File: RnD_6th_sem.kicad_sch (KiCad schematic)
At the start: 62 parts, among them IC1 2EDF7275KXUMA1, J1 HVDC, J10 MMCX-J-P-H-ST-TH1, J2 PWM, J3 HVDC, J4 Conn_02x05_Odd_Even, J5 5V, J6 5V, J7 GND, J8 GND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

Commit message: Final design
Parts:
- removed J4: Conn_02x05_Odd_Even, 61201021621:SHDR10W64P254_2X5_2036X885X925P, symbol Connector_Generic:Conn_02x05_Odd_Even
- added J4: Conn_02x03_Odd_Even, Connector_PinSocket_2.54mm:PinSocket_2x03_P2.54mm_Horizontal, symbol Connector_Generic:Conn_02x03_Odd_Even
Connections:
- net +3.3V: now also J4.1 (Pin_1)
- net GND: now also J4.2 (Pin_2)
- net GND1: now also J4.6 (Pin_6)
- net GND2: now also J4.4 (Pin_4)
- net VCCA: now also J4.5 (Pin_5)
- net VCCB: now also J4.3 (Pin_3)
- no-connect marks 4 -> 0

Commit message: updated the SLDO conn.
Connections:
- net GND: no longer IC1.4 (SLDON)
- no-connect marks 0 -> 1
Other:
- note removed: "Test points: 1. for both current sense resistors 2. High side gan, between them, low side of gan"
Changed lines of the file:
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@@
   (junction (at 177.8 37.465) (diameter 0) (color 0 0 0 0)
   )
+  (no_connect (at 121.285 37.465))
   (wire (pts (xy 98.425 130.175) (xy 101.6 130.175))
     (stroke (width 0) (type default))
@@
     (stroke (width 0) (type default))
   )
-  (wire (pts (xy 97.155 37.465) (xy 121.285 37.465))
-    (stroke (width 0) (type default))
-  )
   (wire (pts (xy 183.515 35.56) (xy 183.515 37.465))
     (stroke (width 0) (type default))
@@
     (stroke (width 0) (type default))
   )
-  (text "Test points: \n1. for both current sense resistors\n2. High side gan, between them, low side of gan\n"
-    (at 221.615 149.225 0)
-    (effects (font (size 1.27 1.27)) (justify left bottom))
-  )
   (text "LEDs" (at 31.75 69.215 0)

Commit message: changed TPs location
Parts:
- added TP6: TestPoint_Alt, TestPoint:TestPoint_Keystone_5000-5004_Miniature, symbol Connector:TestPoint_Alt
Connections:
- net GND3: now also TP6.1
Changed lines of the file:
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@@
   (junction (at 132.08 107.315) (diameter 0) (color 0 0 0 0)
+  )
+  (junction (at 167.005 151.13) (diameter 0) (color 0 0 0 0)
   )
   (junction (at 98.425 133.985) (diameter 0) (color 0 0 0 0)
@@
     (stroke (width 0) (type default))
   )
+  (wire (pts (xy 167.005 151.13) (xy 167.005 157.48))
+    (stroke (width 0) (type default))
+  )
   (wire (pts (xy 192.405 52.705) (xy 198.12 52.705))
     (stroke (width 0) (type default))
@@
     (stroke (width 0) (type default))
   )
-  (wire (pts (xy 167.005 99.06) (xy 167.005 157.48))
+  (wire (pts (xy 167.005 99.06) (xy 167.005 151.13))
     (stroke (width 0) (type default))
   )
@@
         )
       )
+    )
+  )
+  (symbol (lib_id "Connector:TestPoint_Alt") (at 167.005 151.13 270) (unit 1)
+    (in_bom yes) (on_board yes) (dnp no)
+    (property "Reference" "TP6" (at 168.91 153.035 0)
+      (effects (font (size 1.27 1.27)))
+    )
+    (property "Value" "TestPoint_Alt" (at 172.085 153.035 0)
+      (effects (font (size 1.27 1.27)))
+    )
+    (property "Footprint" "TestPoint:TestPoint_Keystone_5000-5004_Miniature" (at 167.005 156.21 0)
+      (effects (font (size 1.27 1.27)) hide)
+    )
+    (property "Datasheet" "~" (at 167.005 156.21 0)
+      (effects (font (size 1.27 1.27)) hide)
+    )
+    (pin "1")
+    (instances
+      (project "RnD_6th_sem"
+        (path "/e0db39ed-81d4-46dc-8309-08feb30c928c"
+          (reference "TP6") (unit 1)
+        )
+      )

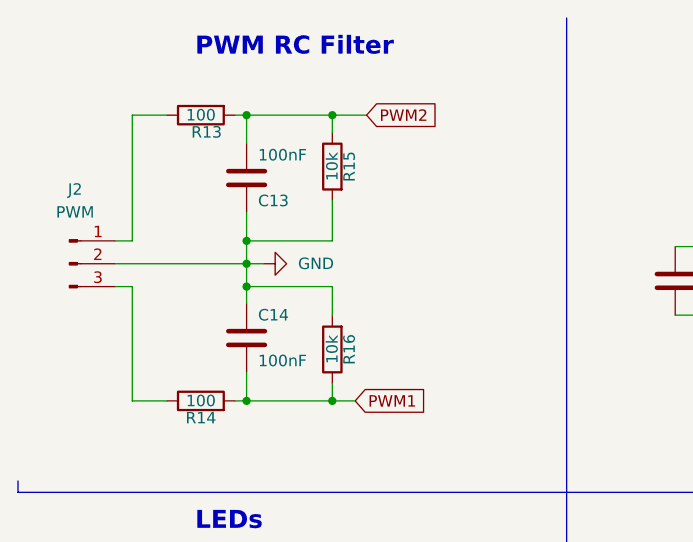
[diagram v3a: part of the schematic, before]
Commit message: changed cap values
PWM RC filter caps changed from 100nF to 0.1nF because of limitations
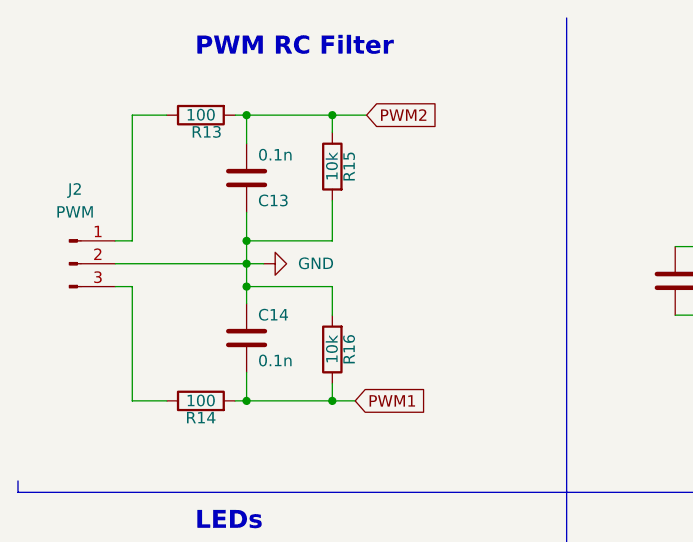
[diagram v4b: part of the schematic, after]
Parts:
- C13, C14: value 100nF -> 0.1n
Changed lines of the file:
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@@
       (effects (font (size 1.27 1.27)) (justify left))
     )
-    (property "Value" "100nF" (at 38.735 27.305 0)
+    (property "Value" "0.1n" (at 38.735 27.305 0)
       (effects (font (size 1.27 1.27)) (justify left))
     )
@@
       (effects (font (size 1.27 1.27)) (justify left))
     )
-    (property "Value" "100nF" (at 38.735 50.165 0)
-      (effects (font (size 1.27 1.27)) (justify left))
-    )
+    (property "Value" "0.1n" (at 38.735 50.165 0)
+      (effects (font (size 1.27 1.27)) (justify left))
+    )
